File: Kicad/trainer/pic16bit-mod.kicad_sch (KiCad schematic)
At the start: 23 parts, among them K301 I2C/GPIO, K303 SPI/GPIO, K304 EUSART/TTL

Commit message: Update
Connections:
- net VDD renamed +VDD
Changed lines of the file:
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@@
     )
   )
-  (symbol (lib_id "tronixio:POWER-VDD") (at 236.22 35.56 0) (unit 1)
+  (symbol (lib_id "tronixio:POWER-+VDD") (at 236.22 35.56 0) (unit 1)
     (in_bom yes) (on_board yes) (dnp no) (fields_autoplaced)
     (property "Reference" "#PWR0151" (at 236.22 45.72 0)
@@
       (effects (font (size 1 1)) hide)
     )
-    (property "Name" "GND" (at 154.94 163.83 0)
-      (effects (font (size 1.15 1.15)) hide)
-    )
     (pin "1")
     (instances
@@
     (property "Datasheet" "" (at 116.84 160.02 0)
       (effects (font (size 1 1)) hide)
-    )
-    (property "Name" "GND" (at 116.84 163.83 0)
-      (effects (font (size 1.15 1.15)) hide)
     )
     (pin "1")
@@
       (effects (font (size 1 1)) hide)
     )
-    (property "Name" "GND" (at 233.68 80.01 0)
-      (effects (font (size 1.15 1.15)) hide)
-    )
     (pin "1")
     (instances
@@
       (effects (font (size 1 1)) hide)
     )
-    (property "Name" "GND" (at 81.28 80.01 0)
-      (effects (font (size 1.15 1.15)) hide)
-    )
     (pin "1")
     (instances
@@
       (effects (font (size 1 1)) hide)
     )
-    (property "Name" "GND" (at 170.18 163.83 0)
-      (effects (font (size 1.15 1.15)) hide)
-    )
     (pin "1")
     (instances
@@
     (property "Datasheet" "" (at 121.92 160.02 0)
       (effects (font (size 1 1)) hide)
-    )
-    (property "Name" "GND" (at 121.92 163.83 0)
-      (effects (font (size 1.15 1.15)) hide)
     )
     (pin "1")
@@
     )
   )
-  (symbol (lib_id "tronixio:POWER-VDD") (at 134.62 116.84 0) (unit 1)
+  (symbol (lib_id "tronixio:POWER-+VDD") (at 134.62 116.84 0) (unit 1)
     (in_bom yes) (on_board yes) (dnp no)
     (property "Reference" "#PWR0163" (at 134.62 127 0)
@@
       (effects (font (size 1 1)) hide)
     )
-    (property "Name" "GND" (at 91.44 80.01 0)
-      (effects (font (size 1.15 1.15)) hide)
-    )
     (pin "1")
     (instances
@@
     )
   )
-  (symbol (lib_id "tronixio:POWER-VDD") (at 99.06 35.56 0) (unit 1)
+  (symbol (lib_id "tronixio:POWER-+VDD") (at 99.06 35.56 0) (unit 1)
     (in_bom yes) (on_board yes) (dnp no) (fields_autoplaced)
     (property "Reference" "#PWR0157" (at 99.06 45.72 0)
@@
       (effects (font (size 1 1)) hide)
     )
-    (property "Name" "GND" (at 218.44 80.01 0)
-      (effects (font (size 1.15 1.15)) hide)
-    )
     (pin "1")
     (instances
@@
       (effects (font (size 1 1)) hide)
     )
-    (property "Name" "GND" (at 228.6 80.01 0)
-      (effects (font (size 1.15 1.15)) hide)
-    )
     (pin "1")
     (instances
@@
       (effects (font (size 1 1)) hide)
     )
-    (property "Name" "GND" (at 160.02 163.83 0)
-      (effects (font (size 1.15 1.15)) hide)
-    )
     (pin "1")
     (instances
@@
       (effects (font (size 1 1)) hide)
     )
-    (property "Name" "GND" (at 223.52 80.01 0)
-      (effects (font (size 1.15 1.15)) hide)
-    )
     (pin "1")
     (instances
@@
     (property "Datasheet" "" (at 149.86 160.02 0)
       (effects (font (size 1 1)) hide)
-    )
-    (property "Name" "GND" (at 149.86 163.83 0)
-      (effects (font (size 1.15 1.15)) hide)
     )
     (pin "1")
@@
       (effects (font (size 1 1)) hide)
     )
-    (property "Name" "GND" (at 132.08 163.83 0)
-      (effects (font (size 1.15 1.15)) hide)
-    )
     (pin "1")
     (instances
@@
     (property "Datasheet" "" (at 213.36 76.2 0)
       (effects (font (size 1 1)) hide)
-    )
-    (property "Name" "GND" (at 213.36 80.01 0)
-      (effects (font (size 1.15 1.15)) hide)
     )
     (pin "1")
@@
       (effects (font (size 1 1)) hide)
     )
-    (property "Name" "GND" (at 76.2 80.01 0)
-      (effects (font (size 1.15 1.15)) hide)
-    )
     (pin "1")
     (instances
@@
     )
   )
-  (symbol (lib_id "tronixio:POWER-VDD") (at 147.32 116.84 0) (unit 1)
+  (symbol (lib_id "tronixio:POWER-+VDD") (at 147.32 116.84 0) (unit 1)
     (in_bom yes) (on_board yes) (dnp no) (fields_autoplaced)
     (property "Reference" "#PWR0164" (at 147.32 127 0)
@@
     (property "Datasheet" "" (at 165.1 160.02 0)
       (effects (font (size 1 1)) hide)
-    )
-    (property "Name" "GND" (at 165.1 163.83 0)
-      (effects (font (size 1.15 1.15)) hide)
     )
     (pin "1")
@@
       (effects (font (size 1 1)) hide)
     )
-    (property "Name" "GND" (at 111.76 163.83 0)
-      (effects (font (size 1.15 1.15)) hide)
-    )
     (pin "1")
     (instances
@@
     (property "Datasheet" "" (at 86.36 76.2 0)
       (effects (font (size 1 1)) hide)
-    )
-    (property "Name" "GND" (at 86.36 80.01 0)
-      (effects (font (size 1.15 1.15)) hide)
     )
     (pin "1")
@@
     (property "Datasheet" "" (at 127 160.02 0)
       (effects (font (size 1 1)) hide)
-    )
-    (property "Name" "GND" (at 127 163.83 0)
-      (effects (font (size 1.15 1.15)) hide)
     )
     (pin "1")
@@
       (effects (font (size 1 1)) hide)
     )
-    (property "Name" "GND" (at 96.52 80.01 0)
-      (effects (font (size 1.15 1.15)) hide)
-    )
-    (pin "1")
+    (pin "1")

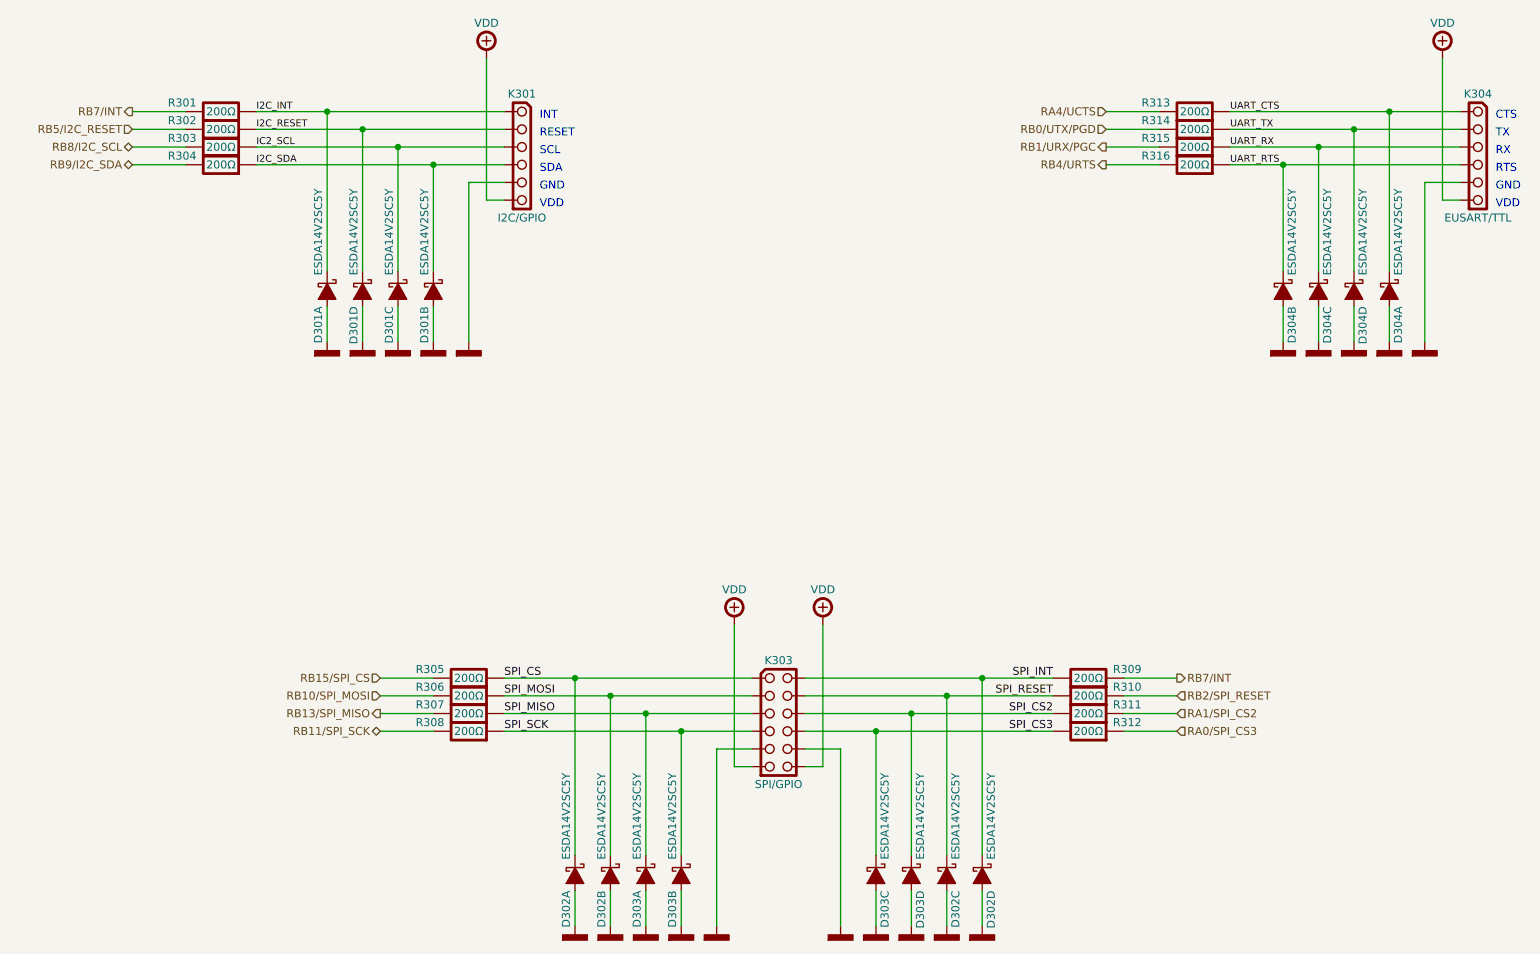
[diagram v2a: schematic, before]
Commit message: Update Trainer Kicad 8
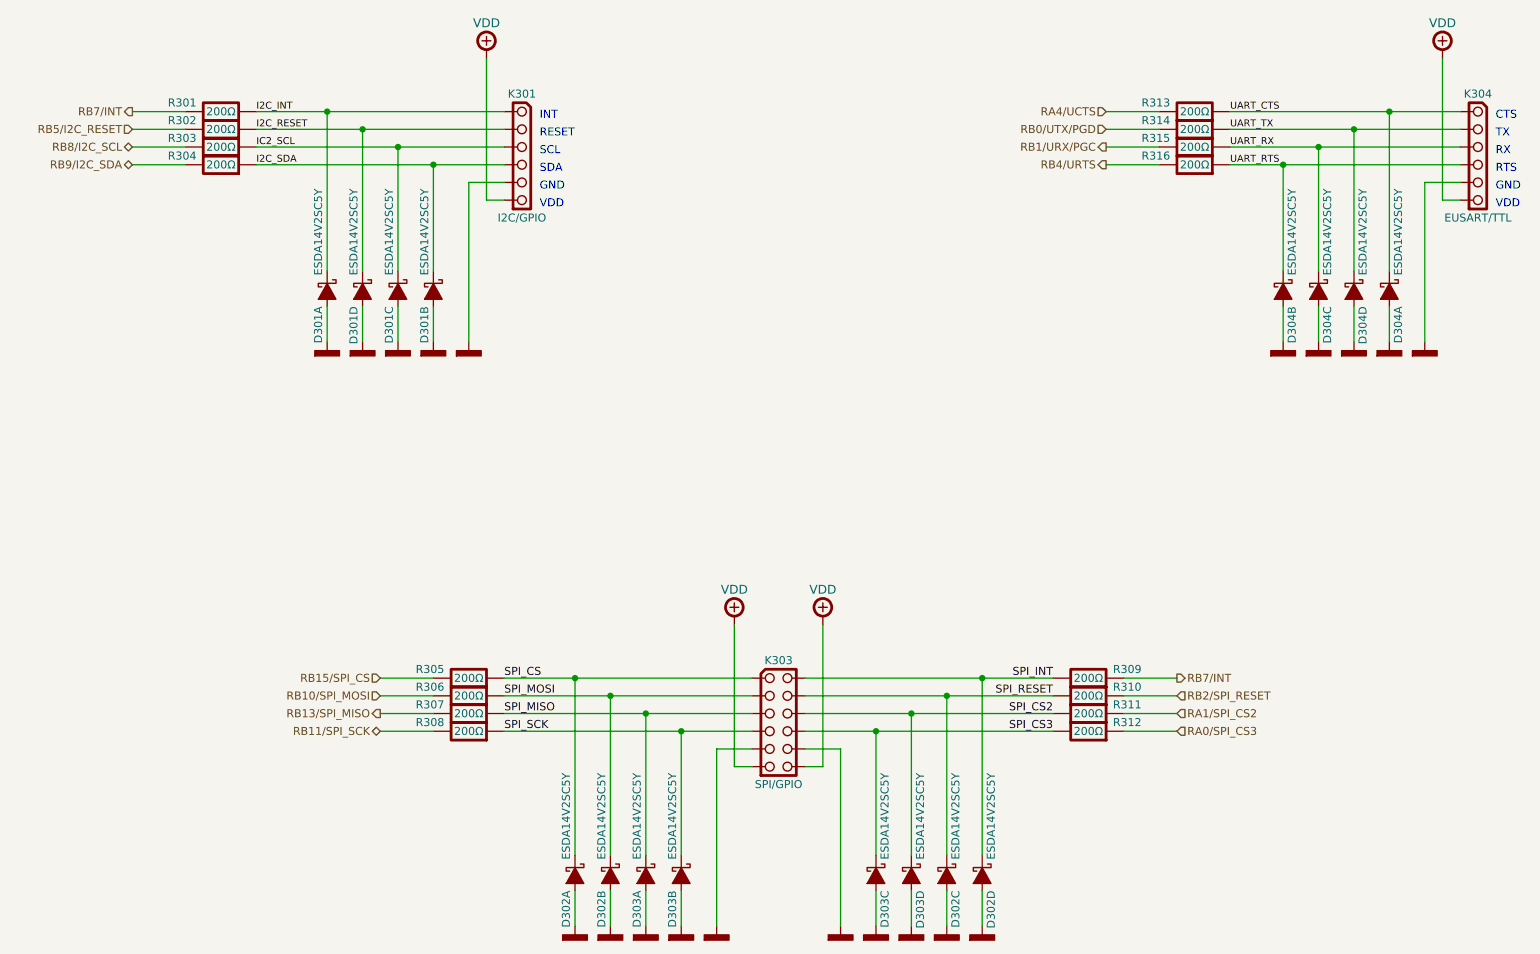
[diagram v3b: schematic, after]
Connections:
- net +VDD renamed POWER-VDD
- net GND renamed POWER-GND

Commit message: Up
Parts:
- K301, K304: symbol tronixio:SAMTEC-SSW-106-02-T-S-RA -> tronixio:SAMTEC-254-F-1X06-RIGHT-ANGLE; Mouser 200-SSW10602TSRA -> 200-SSW10603TSRA
- K303: symbol tronixio:SAMTEC-SSW-106-02-T-D-RA -> tronixio:SAMTEC-254-F-2X06-RIGHT-ANGLE
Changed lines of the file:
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@@
 	)
 	(symbol
-		(lib_id "tronixio:SAMTEC-SSW-106-02-T-S-RA")
+		(lib_id "tronixio:SAMTEC-254-F-1X06-RIGHT-ANGLE")
 		(at 241.3 43.18 0)
 		(unit 1)
@@
 			)
 		)
-		(property "Mouser" "200-SSW10602TSRA"
+		(property "Mouser" "200-SSW10603TSRA"
 			(at 241.3 66.04 0)
 			(effects
@@
 	)
 	(symbol
-		(lib_id "tronixio:SAMTEC-SSW-106-02-T-S-RA")
+		(lib_id "tronixio:SAMTEC-254-F-1X06-RIGHT-ANGLE")
 		(at 104.14 43.18 0)
 		(unit 1)
@@
 			)
 		)
-		(property "Mouser" "200-SSW10602TSRA"
+		(property "Mouser" "200-SSW10603TSRA"
 			(at 104.14 66.04 0)
 			(effects
@@
 	)
 	(symbol
-		(lib_id "tronixio:SAMTEC-SSW-106-02-T-D-RA")
+		(lib_id "tronixio:SAMTEC-254-F-2X06-RIGHT-ANGLE")
 		(at 139.7 124.46 0)
 		(unit 1)
